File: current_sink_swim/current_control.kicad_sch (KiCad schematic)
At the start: 7 parts, among them Q1 BUK9575, U1 LMV358

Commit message: re-annotate schematic
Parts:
- renumbered R6 to R2
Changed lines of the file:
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@@
 (kicad_sch (version 20230121) (generator eeschema)
   (paper "A4")
+  (junction (at 119.507 67.945) (diameter 0) (color 0 0 0 0)
+  )
+  (junction (at 155.575 87.63) (diameter 0) (color 0 0 0 0)
+  )
   (junction (at 113.665 99.06) (diameter 0) (color 0 0 0 0)
   )
-  (junction (at 155.575 87.63) (diameter 0) (color 0 0 0 0)
-  )
   (junction (at 164.465 122.555) (diameter 0) (color 0 0 0 0)
   )
@@
     (stroke (width 0) (type default))
   )
-  (wire (pts (xy 117.475 67.945) (xy 117.475 95.25))
-    (stroke (width 0) (type default))
-  )
-  (wire (pts (xy 117.475 67.945) (xy 123.19 67.945))
+  (wire (pts (xy 117.475 67.945) (xy 119.507 67.945))
     (stroke (width 0) (type default))
   )
@@
     (stroke (width 0) (type default))
   )
+  (wire (pts (xy 117.475 69.596) (xy 119.507 69.596))
+    (stroke (width 0) (type default))
+  )
+  (wire (pts (xy 119.507 67.945) (xy 123.19 67.945))
+    (stroke (width 0) (type default))
+  )
   (wire (pts (xy 164.465 67.945) (xy 168.91 67.945))
     (stroke (width 0) (type default))
   )
+  (wire (pts (xy 164.465 99.06) (xy 164.465 109.855))
+    (stroke (width 0) (type default))
+  )
+  (wire (pts (xy 155.575 87.63) (xy 155.575 60.96))
+    (stroke (width 0) (type default))
+  )
+  (wire (pts (xy 113.665 113.03) (xy 113.665 122.555))
+    (stroke (width 0) (type default))
+  )
+  (wire (pts (xy 164.465 130.175) (xy 174.625 130.175))
+    (stroke (width 0) (type default))
+  )
+  (wire (pts (xy 142.24 87.63) (xy 146.05 87.63))
+    (stroke (width 0) (type default))
+  )
+  (wire (pts (xy 164.465 67.945) (xy 164.465 82.55))
+    (stroke (width 0) (type default))
+  )
+  (wire (pts (xy 132.08 67.945) (xy 132.08 80.01))
+    (stroke (width 0) (type default))
+  )
+  (wire (pts (xy 121.285 85.09) (xy 127 85.09))
+    (stroke (width 0) (type default))
+  )
+  (wire (pts (xy 117.475 95.25) (xy 117.475 69.596))
+    (stroke (width 0) (type default))
+  )
   (wire (pts (xy 113.665 99.06) (xy 121.285 99.06))
     (stroke (width 0) (type default))
   )
-  (wire (pts (xy 164.465 99.06) (xy 164.465 109.855))
-    (stroke (width 0) (type default))
-  )
-  (wire (pts (xy 155.575 87.63) (xy 155.575 60.96))
-    (stroke (width 0) (type default))
-  )
-  (wire (pts (xy 113.665 113.03) (xy 113.665 122.555))
-    (stroke (width 0) (type default))
-  )
-  (wire (pts (xy 164.465 130.175) (xy 174.625 130.175))
-    (stroke (width 0) (type default))
-  )
-  (wire (pts (xy 142.24 87.63) (xy 146.05 87.63))
-    (stroke (width 0) (type default))
-  )
-  (wire (pts (xy 164.465 67.945) (xy 164.465 82.55))
-    (stroke (width 0) (type default))
-  )
-  (wire (pts (xy 132.08 67.945) (xy 132.08 80.01))
-    (stroke (width 0) (type default))
-  )
-  (wire (pts (xy 121.285 85.09) (xy 127 85.09))
-    (stroke (width 0) (type default))
-  )
   (wire (pts (xy 155.575 87.63) (xy 156.845 87.63))
     (stroke (width 0) (type default))
@@
   )
   (wire (pts (xy 132.08 95.25) (xy 132.08 104.775))
+    (stroke (width 0) (type default))
+  )
+  (wire (pts (xy 119.507 69.596) (xy 119.507 67.945))
     (stroke (width 0) (type default))
   )
@@
   (symbol (lib_id "Device:R") (at 149.86 87.63 90) (unit 1)
     (in_bom yes) (on_board yes) (dnp no) (fields_autoplaced)
-    (property "Reference" "R6" (at 149.86 81.28 90)
+    (property "Reference" "R2" (at 149.86 81.28 90)
       (effects (font (size 1.27 1.27)))
     )
@@
       (project "current_sink_swim"
         (path "/d8f9bd22-1078-406d-bafe-f69bb2710c23/7bb47634-abd5-40f7-90e5-fb54860f3e74"
-          (reference "R6") (unit 1)
+          (reference "R2") (unit 1)
         )
       )
@@
         )
         (path "/d8f9bd22-1078-406d-bafe-f69bb2710c23/7bb47634-abd5-40f7-90e5-fb54860f3e74"
-          (reference "C3") (unit 1)
+          (reference "C1") (unit 1)
         )
       )
@@
         )
         (path "/d8f9bd22-1078-406d-bafe-f69bb2710c23/7bb47634-abd5-40f7-90e5-fb54860f3e74"
-          (reference "#PWR01") (unit 1)
+          (reference "#PWR04") (unit 1)
         )
       )
@@
         )
         (path "/d8f9bd22-1078-406d-bafe-f69bb2710c23/7bb47634-abd5-40f7-90e5-fb54860f3e74"
-          (reference "#PWR02") (unit 1)
-        )
-      )
+          (reference "#PWR05") (unit 1)
+        )
+      )

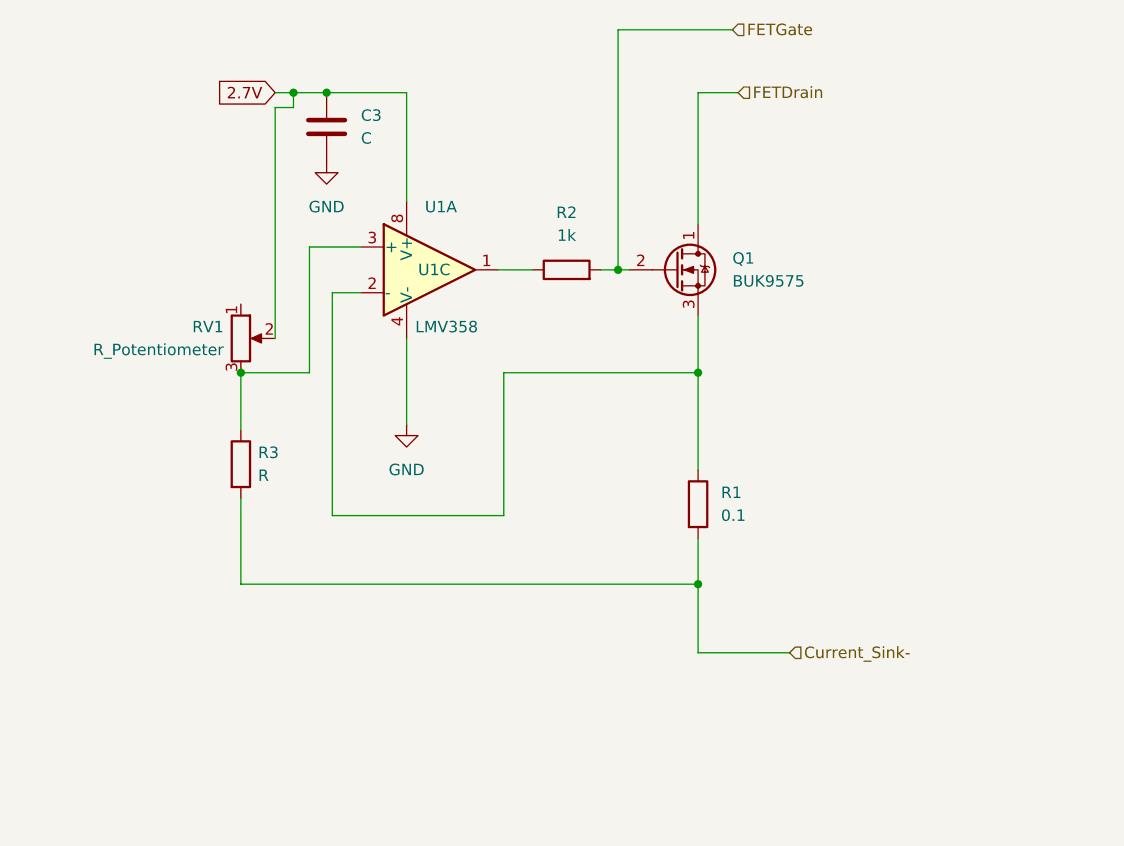
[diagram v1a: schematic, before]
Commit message: assign footprints and start layout
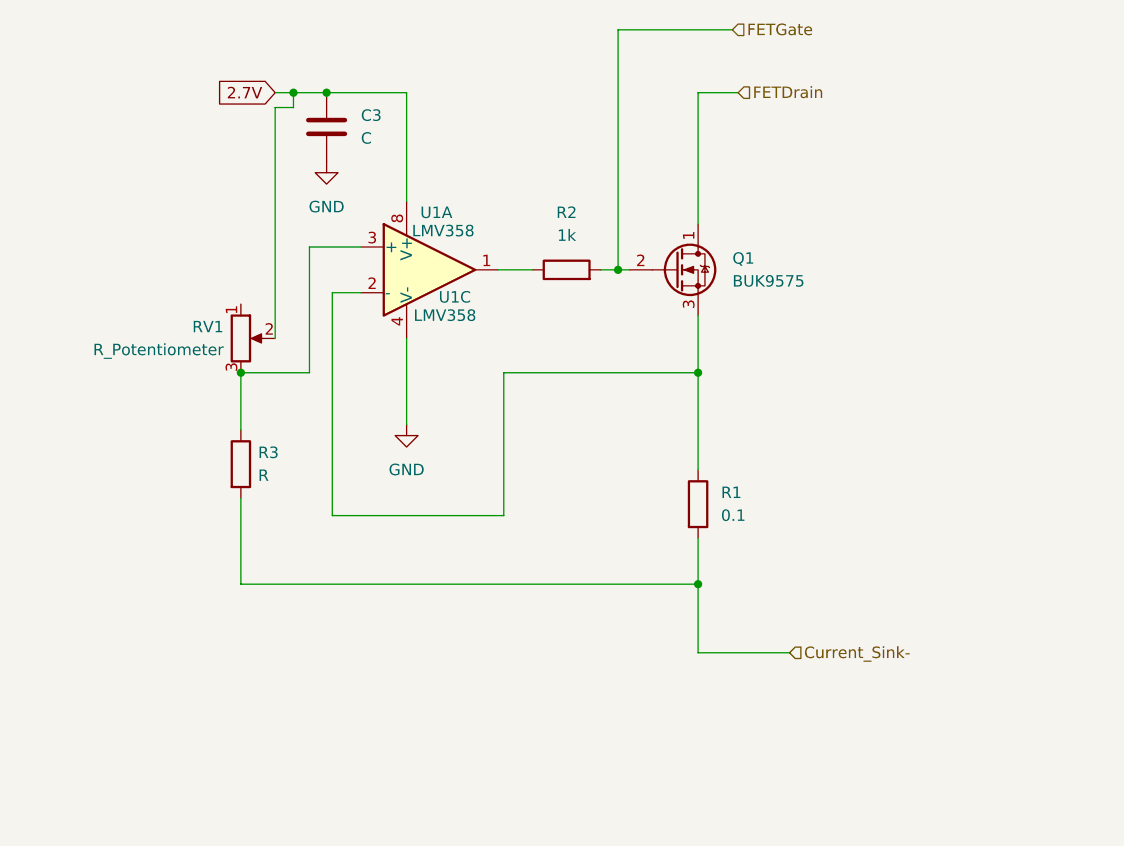
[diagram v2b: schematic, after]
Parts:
- C3: footprint (none) -> Capacitor_SMD:C_0805_2012Metric_Pad1.18x1.45mm_HandSolder
- Q1: footprint (none) -> Package_TO_SOT_THT:TO-220-5_P3.4x3.7mm_StaggerEven_Lead3.8mm_Vertical
- R1: footprint (none) -> Resistor_THT:R_Axial_DIN0309_L9.0mm_D3.2mm_P12.70mm_Horizontal
- R2, R3: footprint (none) -> Resistor_SMD:R_0805_2012Metric_Pad1.20x1.40mm_HandSolder
- RV1: footprint (none) -> Package_TO_SOT_THT:TO-220-3_Vertical
- U1: footprint (none) -> Package_SO:SOIC-8_3.9x4.9mm_P1.27mm; MPN (none) -> LMV358IDT

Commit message: add heat sink
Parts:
- added J4: Conn_01x01_Pin, custom_modules:FAT-220, symbol Connector:Conn_01x01_Pin
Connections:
- no-connect marks 0 -> 1
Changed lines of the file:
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@@
   (junction (at 123.19 67.945) (diameter 0) (color 0 0 0 0)
   )
+  (no_connect (at 205.232 99.314))
   (wire (pts (xy 153.67 87.63) (xy 155.575 87.63))
     (stroke (width 0) (type default))
@@
         )
       )
+    )
+  )
+  (symbol (lib_id "Connector:Conn_01x01_Pin") (at 200.152 99.314 0) (unit 1)
+    (in_bom yes) (on_board yes) (dnp no) (fields_autoplaced)
+    (property "Reference" "J4" (at 200.787 93.98 0)
+      (effects (font (size 1.27 1.27)))
+    )
+    (property "Value" "Conn_01x01_Pin" (at 200.787 96.52 0)
+      (effects (font (size 1.27 1.27)))
+    )
+    (property "Footprint" "custom_modules:FAT-220" (at 200.152 99.314 0)
+      (effects (font (size 1.27 1.27)) hide)
+    )
+    (property "Datasheet" "~" (at 200.152 99.314 0)
+      (effects (font (size 1.27 1.27)) hide)
+    )
+    (pin "1")
+    (instances
+      (project "current_sink_swim"
+        (path "/d8f9bd22-1078-406d-bafe-f69bb2710c23/7bb47634-abd5-40f7-90e5-fb54860f3e74"
+          (reference "J4") (unit 1)
+        )
+      )

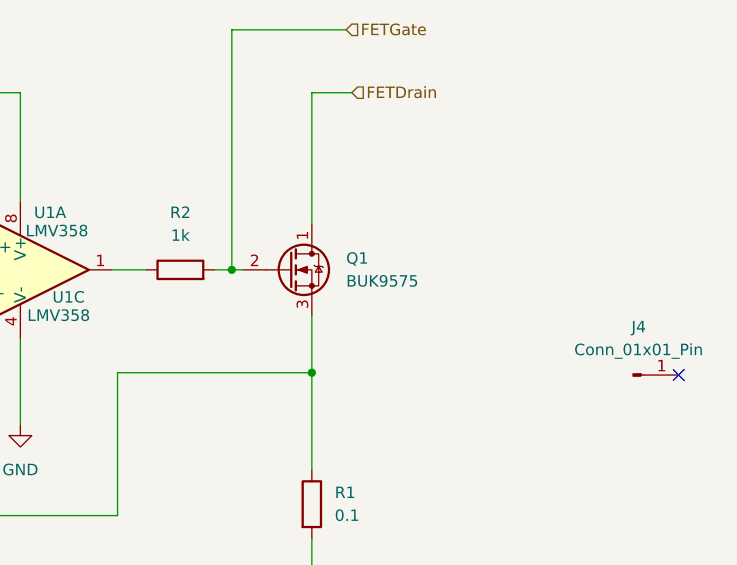
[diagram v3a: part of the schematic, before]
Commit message: created a rough board outline
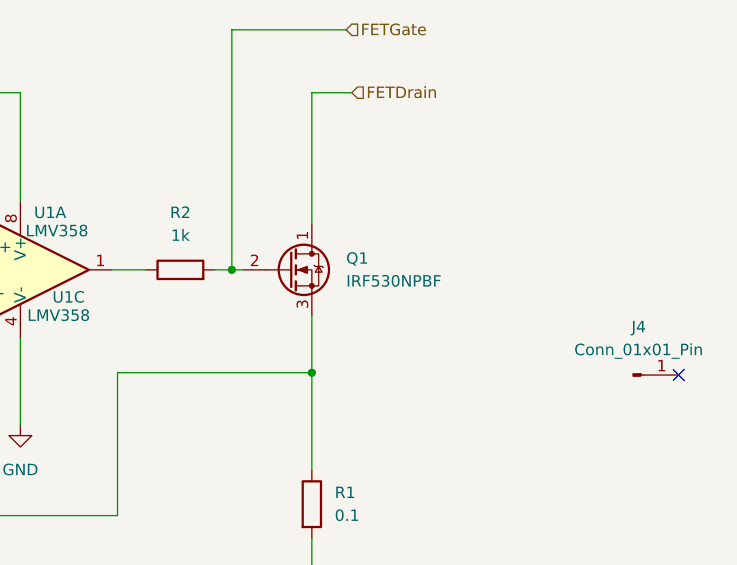
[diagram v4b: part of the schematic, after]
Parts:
- Q1: value BUK9575 -> IRF530NPBF; footprint Package_TO_SOT_THT:TO-220-5_P3.4x3.7mm_StaggerEven_Lead3.8mm_Vertical -> Package_TO_SOT_THT:TO-220-3_Vertical; MPN BUK9575-100A, 127 -> IRF530NPBF
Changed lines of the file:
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@@
       (effects (font (size 1.27 1.27)) (justify left))
     )
-    (property "Value" "BUK9575" (at 168.275 88.9 0)
+    (property "Value" "IRF530NPBF" (at 168.275 88.9 0)
       (effects (font (size 1.27 1.27)) (justify left))
     )
-    (property "Footprint" "Package_TO_SOT_THT:TO-220-5_P3.4x3.7mm_StaggerEven_Lead3.8mm_Vertical" (at 167.005 85.09 0)
+    (property "Footprint" "Package_TO_SOT_THT:TO-220-3_Vertical" (at 167.005 85.09 0)
       (effects (font (size 1.27 1.27)) hide)
     )
-    (property "Datasheet" "~" (at 161.925 87.63 0)
+    (property "Datasheet" "https://www.infineon.com/dgdl/irf530npbf.pdf?fileId=5546d462533600a4015355e386b1199a" (at 161.925 87.63 0)
       (effects (font (size 1.27 1.27)) hide)
     )
-    (property "MPN" "BUK9575-100A, 127" (at 161.925 87.63 0)
+    (property "MPN" "IRF530NPBF" (at 161.925 87.63 0)
       (effects (font (size 1.27 1.27)) hide)
     )
@@
       (effects (font (size 1.27 1.27)) hide)
     )
+    (property "MPN" "" (at 200.152 99.314 0)
+      (effects (font (size 1.27 1.27)) hide)
+    )

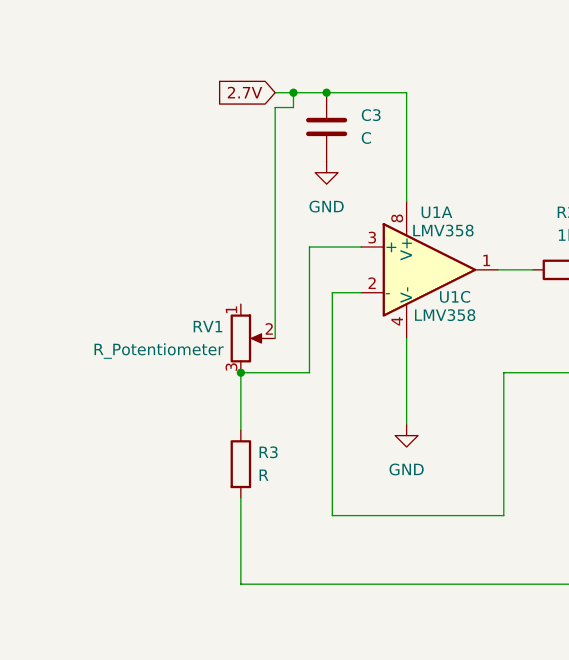
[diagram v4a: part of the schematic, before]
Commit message: add correct pot symbols
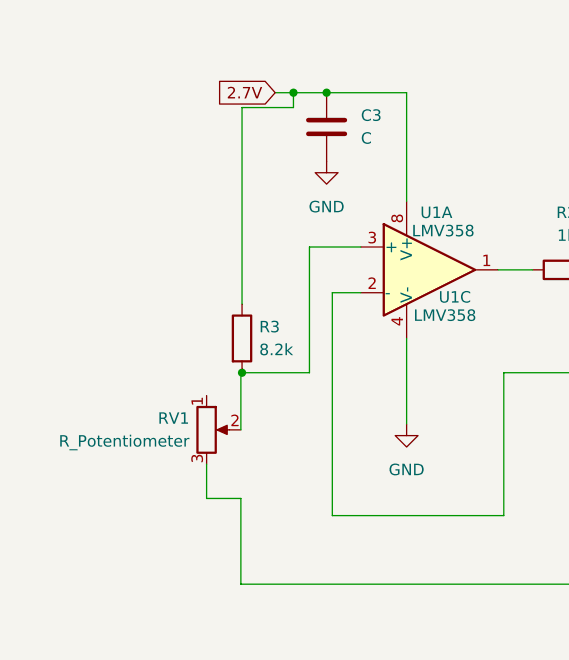
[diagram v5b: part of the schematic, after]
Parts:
- R3: value R -> 8.2k
- RV1: footprint Package_TO_SOT_THT:TO-220-3_Vertical -> Potentiometer_THT:Potentiometer_Bourns_PTV09A-2_Single_Horizontal
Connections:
- net 2.7V: now also R3.1; no longer RV1.2
- net Current_Sink-: now also RV1.3; no longer R3.2
- new net: R3.2, RV1.2, U1.3 (+)
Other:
- moved on the sheet: R3, RV1
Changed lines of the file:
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@@
   (junction (at 119.507 67.945) (diameter 0) (color 0 0 0 0)
   )
+  (junction (at 113.792 99.06) (diameter 0) (color 0 0 0 0)
+  )
   (junction (at 155.575 87.63) (diameter 0) (color 0 0 0 0)
-  )
-  (junction (at 113.665 99.06) (diameter 0) (color 0 0 0 0)
   )
   (junction (at 164.465 122.555) (diameter 0) (color 0 0 0 0)
@@
     (stroke (width 0) (type default))
   )
+  (wire (pts (xy 113.792 69.596) (xy 113.792 91.44))
+    (stroke (width 0) (type default))
+  )
   (wire (pts (xy 127 90.17) (xy 123.825 90.17))
     (stroke (width 0) (type default))
@@
     (stroke (width 0) (type default))
   )
+  (wire (pts (xy 109.855 113.03) (xy 109.855 109.22))
+    (stroke (width 0) (type default))
+  )
   (wire (pts (xy 117.475 67.945) (xy 119.507 67.945))
     (stroke (width 0) (type default))
@@
     (stroke (width 0) (type default))
   )
-  (wire (pts (xy 117.475 69.596) (xy 119.507 69.596))
+  (wire (pts (xy 113.792 69.596) (xy 119.507 69.596))
     (stroke (width 0) (type default))
   )
@@
     (stroke (width 0) (type default))
   )
+  (wire (pts (xy 113.665 113.03) (xy 109.855 113.03))
+    (stroke (width 0) (type default))
+  )
   (wire (pts (xy 164.465 130.175) (xy 174.625 130.175))
     (stroke (width 0) (type default))
@@
     (stroke (width 0) (type default))
   )
-  (wire (pts (xy 117.475 95.25) (xy 117.475 69.596))
-    (stroke (width 0) (type default))
-  )
-  (wire (pts (xy 113.665 99.06) (xy 121.285 99.06))
+  (wire (pts (xy 113.665 99.06) (xy 113.792 99.06))
     (stroke (width 0) (type default))
   )
@@
   )
   (wire (pts (xy 132.08 95.25) (xy 132.08 104.775))
+    (stroke (width 0) (type default))
+  )
+  (wire (pts (xy 113.792 99.06) (xy 121.285 99.06))
     (stroke (width 0) (type default))
   )
@@
     (effects (font (size 1.27 1.27)) (justify left))
   )
-  (symbol (lib_id "Device:R") (at 113.665 109.22 0) (unit 1)
-    (in_bom yes) (on_board yes) (dnp no) (fields_autoplaced)
-    (property "Reference" "R3" (at 115.57 107.95 0)
-      (effects (font (size 1.27 1.27)) (justify left))
-    )
-    (property "Value" "R" (at 115.57 110.49 0)
-      (effects (font (size 1.27 1.27)) (justify left))
-    )
-    (property "Footprint" "Resistor_SMD:R_0805_2012Metric_Pad1.20x1.40mm_HandSolder" (at 111.887 109.22 90)
-      (effects (font (size 1.27 1.27)) hide)
-    )
-    (property "Datasheet" "~" (at 113.665 109.22 0)
+  (symbol (lib_id "Device:R") (at 113.792 95.25 0) (unit 1)
+    (in_bom yes) (on_board yes) (dnp no) (fields_autoplaced)
+    (property "Reference" "R3" (at 115.697 93.98 0)
+      (effects (font (size 1.27 1.27)) (justify left))
+    )
+    (property "Value" "8.2k" (at 115.697 96.52 0)
+      (effects (font (size 1.27 1.27)) (justify left))
+    )
+    (property "Footprint" "Resistor_SMD:R_0805_2012Metric_Pad1.20x1.40mm_HandSolder" (at 112.014 95.25 90)
+      (effects (font (size 1.27 1.27)) hide)
+    )
+    (property "Datasheet" "~" (at 113.792 95.25 0)
+      (effects (font (size 1.27 1.27)) hide)
+    )
+    (property "MPN" "" (at 113.792 95.25 0)
       (effects (font (size 1.27 1.27)) hide)
     )
@@
     )
   )
-  (symbol (lib_id "Device:R_Potentiometer") (at 113.665 95.25 0) (unit 1)
-    (in_bom yes) (on_board yes) (dnp no) (fields_autoplaced)
-    (property "Reference" "RV1" (at 111.76 93.98 0)
+  (symbol (lib_id "Device:R_Potentiometer") (at 109.855 105.41 0) (unit 1)
+    (in_bom yes) (on_board yes) (dnp no) (fields_autoplaced)
+    (property "Reference" "RV1" (at 107.95 104.14 0)
       (effects (font (size 1.27 1.27)) (justify right))
     )
-    (property "Value" "R_Potentiometer" (at 111.76 96.52 0)
+    (property "Value" "R_Potentiometer" (at 107.95 106.68 0)
       (effects (font (size 1.27 1.27)) (justify right))
     )
-    (property "Footprint" "Package_TO_SOT_THT:TO-220-3_Vertical" (at 113.665 95.25 0)
-      (effects (font (size 1.27 1.27)) hide)
-    )
-    (property "Datasheet" "~" (at 113.665 95.25 0)
-      (effects (font (size 1.27 1.27)) hide)
-    )
+    (property "Footprint" "Potentiometer_THT:Potentiometer_Bourns_PTV09A-2_Single_Horizontal" (at 109.855 105.41 0)
+      (effects (font (size 1.27 1.27)) hide)
+    )
+    (property "Datasheet" "~" (at 109.855 105.41 0)
+      (effects (font (size 1.27 1.27)) hide)
+    )
+    (property "MPN" "" (at 109.855 105.41 0)
+      (effects (font (size 1.27 1.27)) hide)
+    )

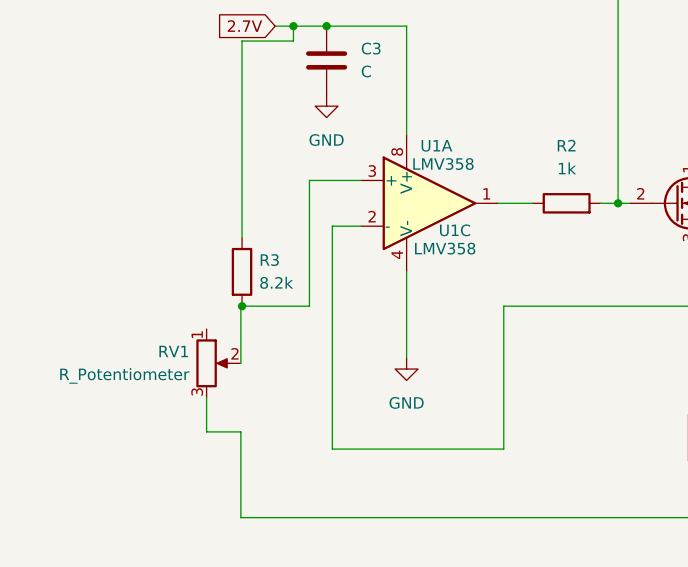
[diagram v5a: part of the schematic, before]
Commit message: clean up potentiometer circuits
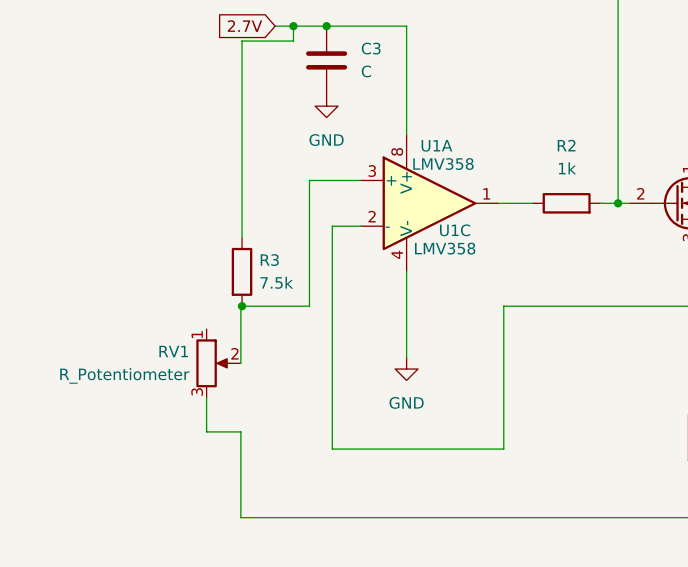
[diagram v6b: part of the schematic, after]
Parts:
- R3: value 8.2k -> 7.5k
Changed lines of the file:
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@@
       (effects (font (size 1.27 1.27)) (justify left))
     )
-    (property "Value" "8.2k" (at 115.697 96.52 0)
+    (property "Value" "7.5k" (at 115.697 96.52 0)
       (effects (font (size 1.27 1.27)) (justify left))
     )
